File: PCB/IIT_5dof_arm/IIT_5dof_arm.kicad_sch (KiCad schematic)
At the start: 62 parts, among them J1 Screw_Terminal_01x02, J2 Conn_01x06, J3 Conn_01x06, J4 Conn_01x06, J5 Conn_01x06, J6 Conn_01x06, J7 Conn_01x06, J9 DE9_Receptacle_MountingHoles, SW1 SW_MAIN, SW15 SW_MOT, SW17 SW_SPDT, SW18 SW_SPDT, SW19 SW_SPDT, SW20 SW_SPDT, SW21 SW_SPDT, SW22 SW_SPDT, SW23 SW_SPDT, SW24 SW_SPDT, SW25 SW_SPDT, SW26 SW_SPDT, SW27 SW_SPDT, SW28 SW_SPDT, U5 XL8574T, U6 MAX3232, U9 4504

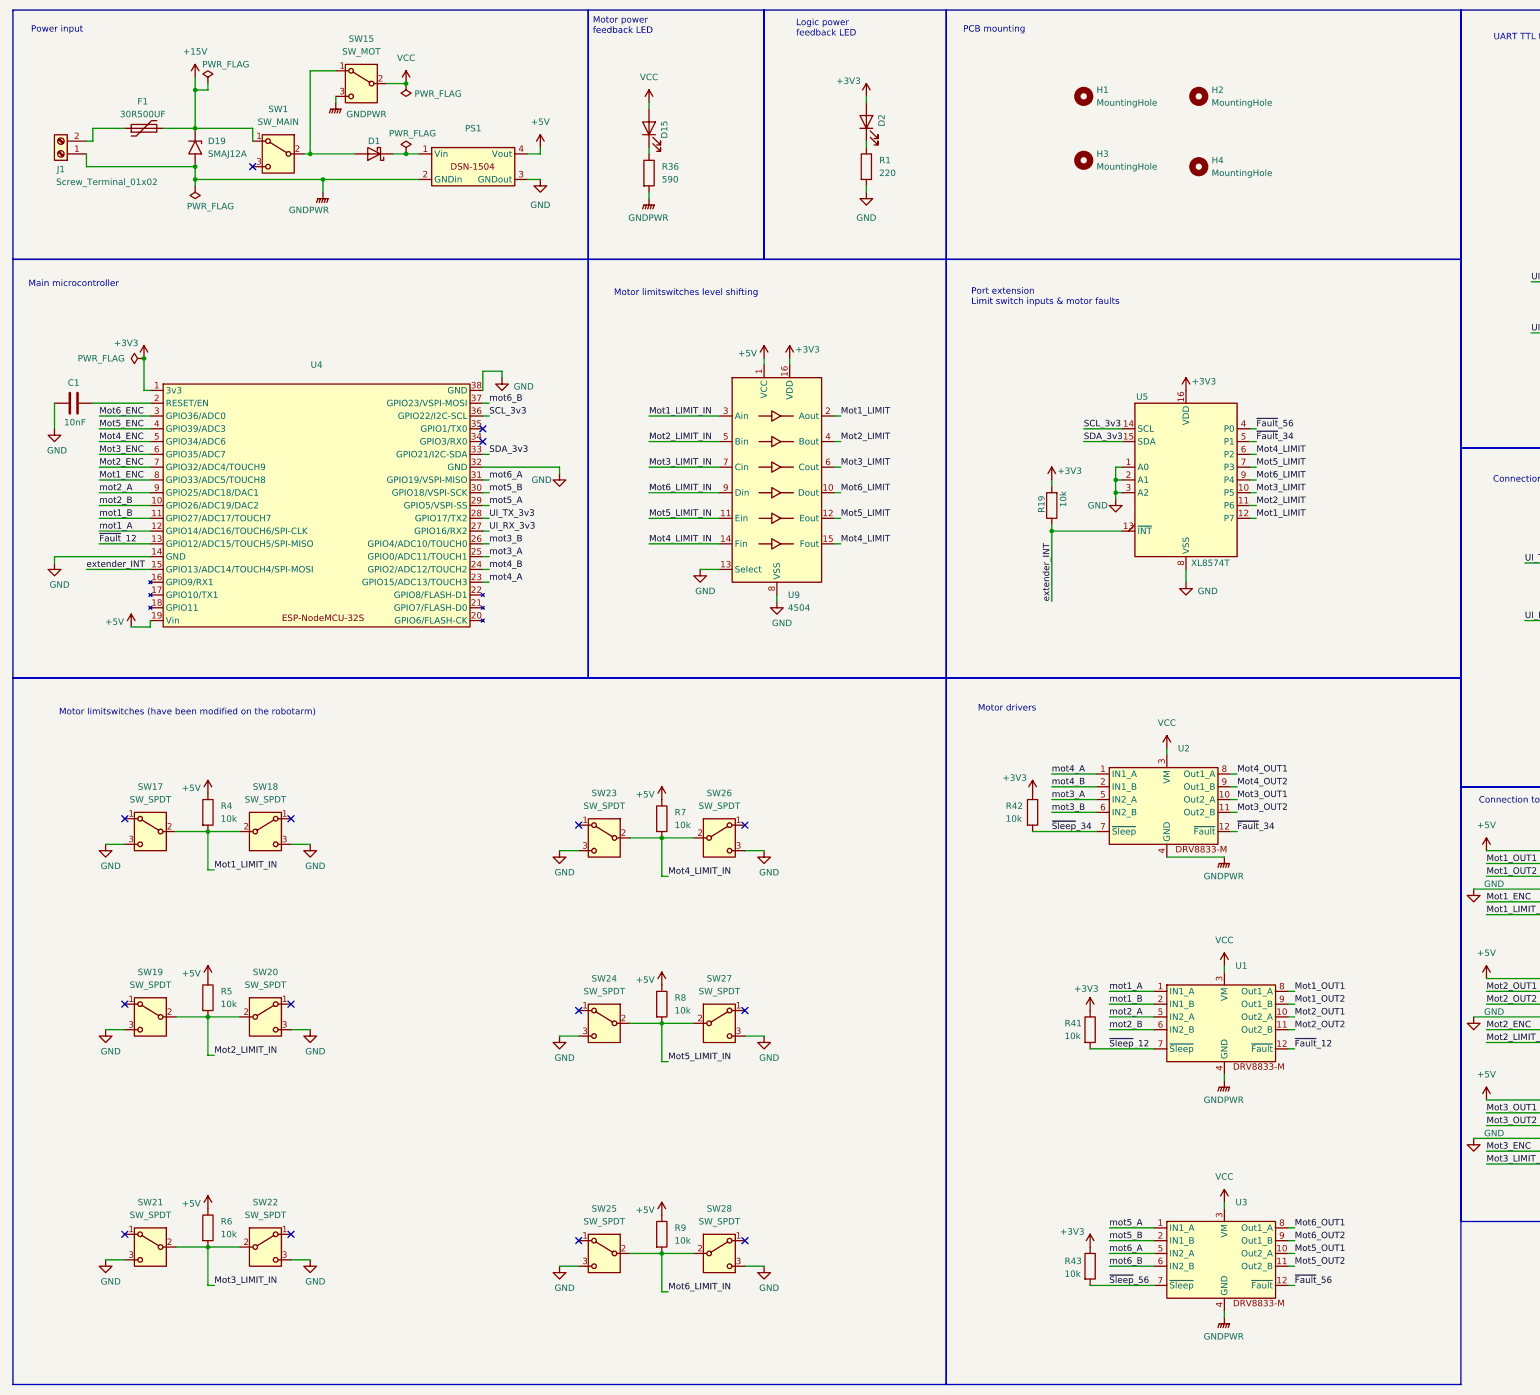
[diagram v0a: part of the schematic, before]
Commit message: Add decoupling capacitors
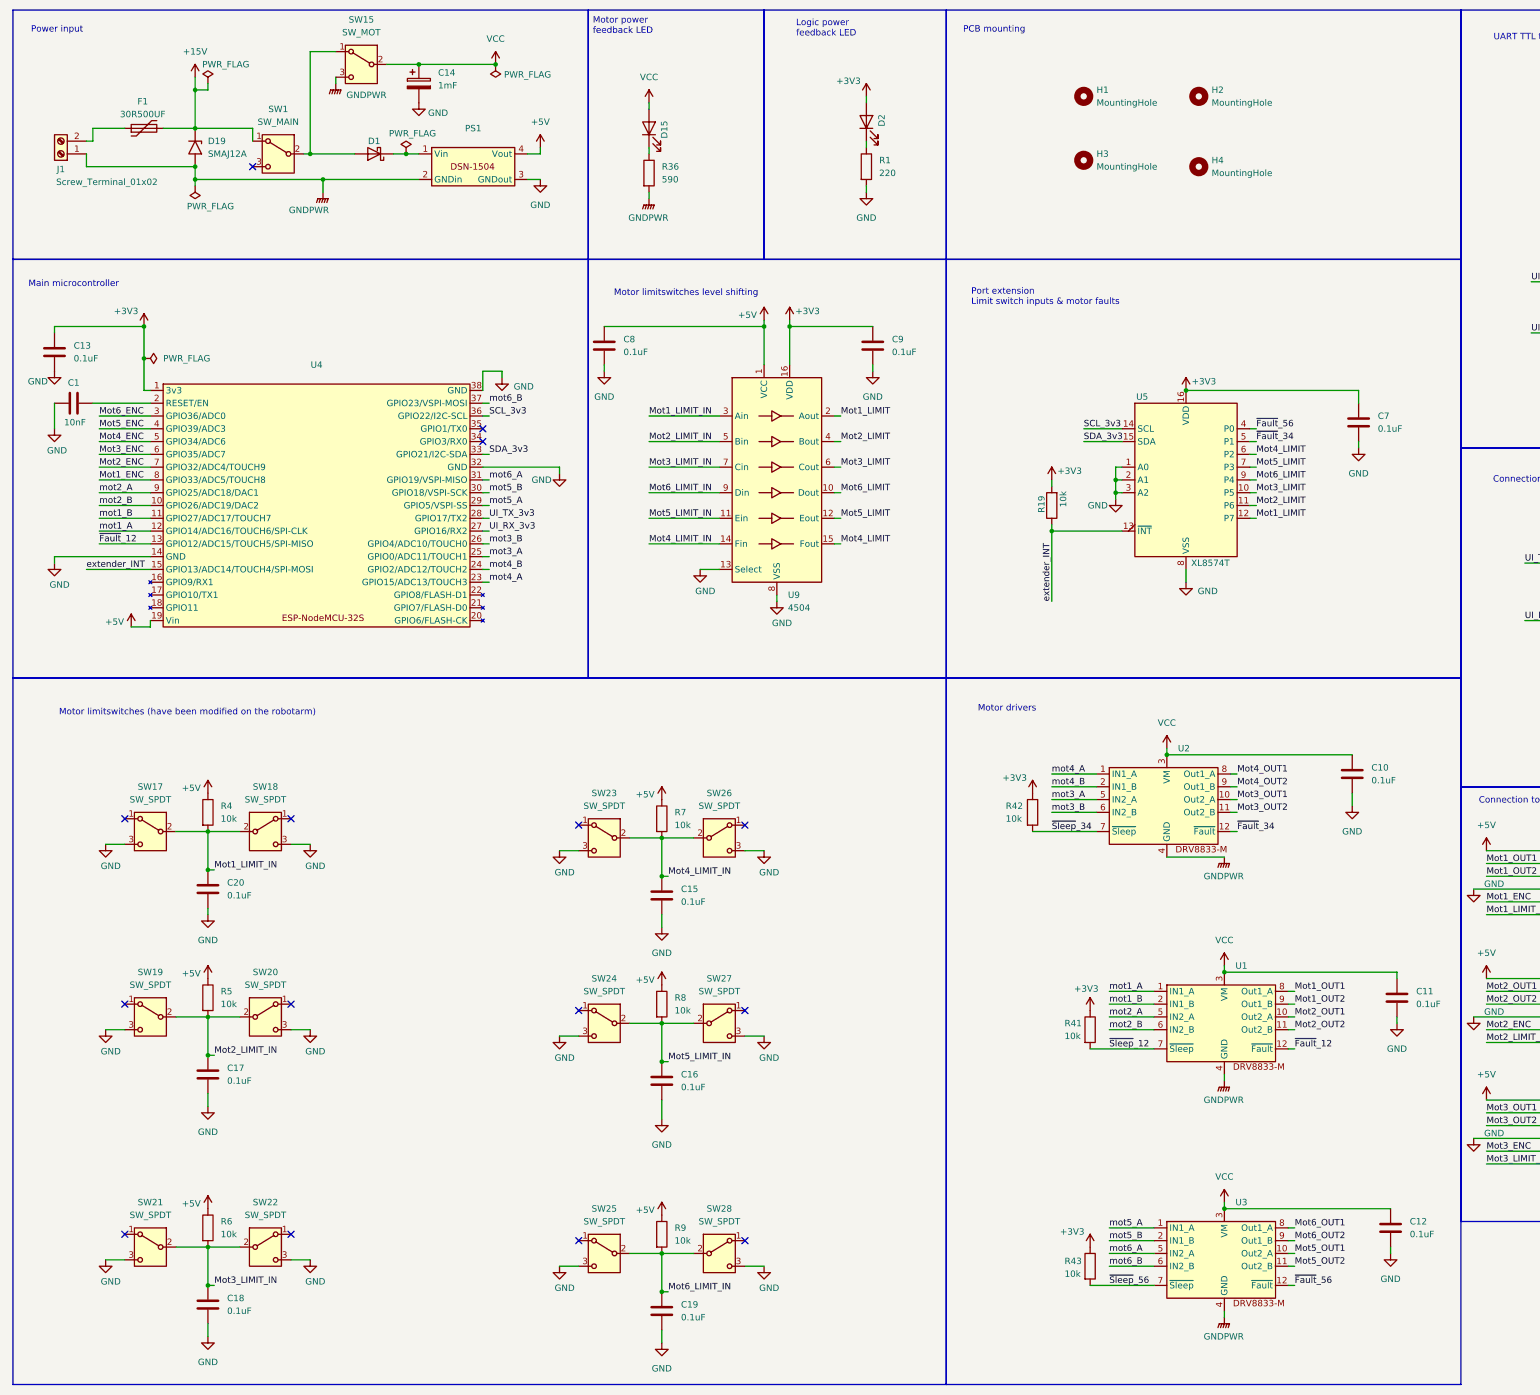
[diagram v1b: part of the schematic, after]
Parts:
- added C10, C11, C12, C13, C15, C16, C17, C18, C19, C20, C7, C8, C9: 0.1uF, Capacitor_SMD:C_0805_2012Metric_Pad1.18x1.45mm_HandSolder, symbol Device:C
- added C14: 1mF, symbol Device:C_Polarized
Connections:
- net +3V3: now also C13.1, C7.1, C9.1
- net +5V: now also C8.1
- net GND: now also C10.2, C11.2, C12.2, C13.2, C14.2, C15.2, C16.2, C17.2, C18.2, C19.2, C20.2, C7.2, C8.2, C9.2
- net Mot1_LIMIT_IN: now also C20.1
- net Mot2_LIMIT_IN: now also C17.1
- net Mot3_LIMIT_IN: now also C18.1
- net Mot4_LIMIT_IN: now also C15.1
- net Mot5_LIMIT_IN: now also C16.1
- net Mot6_LIMIT_IN: now also C19.1
- net VCC: now also C10.1, C11.1, C12.1, C14.1
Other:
- moved on the sheet: SW15

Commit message: Decoupling capacitors layout
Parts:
- C14: value 1mF -> 1000uF; footprint (none) -> Capacitor_THT:C_Radial_D10.0mm_H16.0mm_P5.00mm
- C15, C16, C17, C18, C19, C20: value 0.1uF -> 10nF
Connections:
- net GND: no longer C10.2, C11.2, C12.2, C14.2
- net GNDPWR: now also C10.2, C11.2, C12.2, C14.2

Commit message: Eliminate GNDPWR
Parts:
- C10, C11, C12: value 0.1uF -> 10uF
- D5: value SMAJ12A -> SMAJ5.0A
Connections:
- net GNDPWR is gone; now on net GND: C10.2, C11.2, C12.2, C14.2, D19.2 (A2), J1.1 (Pin_1), PS1.2 (GNDin), R36.2, SW15.3 (C), U1.4 (GND), U2.4 (GND), U3.4 (GND)

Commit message: Update schematic with new functionalities
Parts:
- removed R3: 1k, Resistor_SMD:R_0805_2012Metric_Pad1.20x1.40mm_HandSolder, symbol Device:R
- added C13: 0.1uF, Capacitor_SMD:C_0805_2012Metric_Pad1.18x1.45mm_HandSolder, symbol Device:C
- added D10, D11, D12, D13, D14, D15, D16, D3, D4, D5, D6, D9: LED, LED_THT:LED_D5.0mm, symbol Device:LED
- added J2: Conn_01x02, Connector_PinSocket_2.54mm:PinSocket_1x02_P2.54mm_Vertical, symbol Connector_Generic:Conn_01x02
- added J3: Conn_02x06_Odd_Even, Connector_IDC:IDC-Header_2x06_P2.54mm_Vertical, symbol Connector_Generic:Conn_02x06_Odd_Even
- added J4: Conn_02x08_Odd_Even, Connector_IDC:IDC-Header_2x08_P2.54mm_Vertical, symbol Connector_Generic:Conn_02x08_Odd_Even
- added J5: Conn_02x04_Odd_Even, Connector_IDC:IDC-Header_2x04_P2.54mm_Vertical, symbol Connector_Generic:Conn_02x04_Odd_Even
- added J6: Conn_01x04, Connector_Molex:Molex_KK-254_AE-6410-04A_1x04_P2.54mm_Vertical, symbol Connector_Generic:Conn_01x04
- added K1: G5LE-1, Relay_THT:Relay_SPDT_Omron-G5LE-1, symbol Relay:G5LE-1
- added Q1, Q2: 2N7002, Package_TO_SOT_SMD:SOT-23, symbol Transistor_FET:2N7002
- added R10, R11, R12, R17, R34: 1k, Resistor_SMD:R_0805_2012Metric_Pad1.20x1.40mm_HandSolder, symbol Device:R
- added R13, R16, R29, R31, R33, R9: 10k, Resistor_SMD:R_0805_2012Metric_Pad1.20x1.40mm_HandSolder, symbol Device:R
- added R18, R19, R20, R21, R22, R23: 3k, Resistor_SMD:R_0805_2012Metric_Pad1.20x1.40mm_HandSolder, symbol Device:R
- added R28, R30: 4k7, Resistor_SMD:R_0805_2012Metric_Pad1.20x1.40mm_HandSolder, symbol Device:R
- added R35: 2k, Resistor_SMD:R_0805_2012Metric_Pad1.20x1.40mm_HandSolder, symbol Device:R
- added R7: 220, Resistor_SMD:R_0805_2012Metric_Pad1.20x1.40mm_HandSolder, symbol Device:R
- added R8: 100k, Resistor_SMD:R_0805_2012Metric_Pad1.20x1.40mm_HandSolder, symbol Device:R
- added SW16, SW17: SW_LEVER, symbol Switch:SW_SPST
- added SW8: SW_Push, symbol Switch:SW_Push
- added U2: 74LS157, Package_SO:SO-16_5.3x10.2mm_P1.27mm, symbol 74xx:74LS157
- added U4: XL8574T, Package_SO:SOIC-16W_7.5x10.3mm_P1.27mm, symbol Interface_Expansion:PCF8574
- D7: renamed from D15; footprint Connector_Molex:Molex_KK-254_AE-6410-02A_1x02_P2.54mm_Vertical -> LED_THT:LED_D5.0mm
- D8: renamed from D2; footprint Connector_Molex:Molex_KK-254_AE-6410-02A_1x02_P2.54mm_Vertical -> LED_THT:LED_D5.0mm
- R14: renamed from R36; value 590 -> 10k
- R15: renamed from R1; value 220 -> 1k
- SW12: renamed from SW15; value SW_MOT -> SW_LEVER; footprint Connector_Molex:Molex_KK-254_AE-6410-03A_1x03_P2.54mm_Vertical -> (none)
- SW7: renamed from SW1; value SW_MAIN -> SW_LEVER; footprint Connector_Molex:Molex_KK-254_AE-6410-03A_1x03_P2.54mm_Vertical -> (none)
- U3: renamed from U9; footprint Package_DIP:DIP-16_W7.62mm_Socket_LongPads -> Package_SO:SOIC-16_3.9x9.9mm_P1.27mm
- renumbered C13 to C1, C8 to C10, C9 to C11, C7 to C14, C10 to C15, C11 to C16, C2 to C17, C5 to C18, C6 to C19, C1 to C2, C3 to C20, C4 to C21, C20 to C3, C17 to C4, C18 to C5, C15 to C6, C16 to C7, C19 to C8, C14 to C9, D19 to D1, D4 to D17, D3 to D18, D5 to D19, D1 to D2, J5 to J10, J6 to J11, J7 to J12, J9 to J13, J2 to J7, J3 to J8, J4 to J9, R4 to R1, R5 to R2, R19 to R24, R42 to R25, R41 to R26, R43 to R27, R6 to R3, R2 to R32, R7 to R4, R8 to R5, R9 to R6, SW17 to SW1, SW24 to SW10, SW25 to SW11, SW26 to SW13, SW27 to SW14, SW28 to SW15, SW19 to SW2, SW21 to SW3, SW18 to SW4, SW20 to SW5, SW22 to SW6, SW23 to SW9, U4 to U1, U2 to U6, U1 to U7, U3 to U8, U6 to U9
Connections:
- net +15V: now also J5.1 (Pin_1)
- net +3V3: now also C1.2, C13.1, D3.2 (A), D4.2 (A), D5.2 (A), J3.1 (Pin_1), J3.11 (Pin_11), J3.3 (Pin_3), J3.5 (Pin_5), J3.7 (Pin_7), J3.9 (Pin_9), J4.13 (Pin_13), J4.15 (Pin_15), J4.5 (Pin_5), J4.9 (Pin_9), R28.2, R29.1, R30.2, R31.1, U2.16 (VCC), U4.16 (VDD); no longer C1.1
- net +5V: now also J6.1 (Pin_1), K1.5, R33.1
- net GND: now also C1.1, C13.2, D16.1 (K), J2.2 (Pin_2), J4.12 (Pin_12), J5.6 (Pin_6), J5.8 (Pin_8), J6.4 (Pin_4), Q2.2 (S), R13.2, R16.2, R18.2, R19.2, R20.2, R21.2, R22.2, R23.2, R35.2, R8.2, R9.2, SW16.1 (A), SW17.1 (A), SW8.2, U2.8 (GND), U4.2 (A1), U4.3 (A2), U4.8 (VSS); no longer C1.2, SW12.3 (C)
- net Mot1_ENC: now also U2.13 (I1d), U2.5 (I0b); no longer U1.8 (GPIO33/ADC5/TOUCH8)
- net Mot1_LIMIT_IN: now also D15.2 (A)
- net Mot2_ENC: now also U1.8 (GPIO33/ADC5/TOUCH8); no longer U1.7 (GPIO32/ADC4/TOUCH9)
- net Mot2_LIMIT_IN: now also D14.2 (A)
- net Mot3_ENC: now also U1.7 (GPIO32/ADC4/TOUCH9); no longer U1.6 (GPIO35/ADC7)
- net Mot3_LIMIT_IN: now also D13.2 (A)
- net Mot4_ENC: now also U1.6 (GPIO35/ADC7); no longer U1.5 (GPIO34/ADC6)
- net Mot4_LIMIT_IN: now also D12.2 (A)
- net Mot5_ENC: now also U1.5 (GPIO34/ADC6); no longer U1.4 (GPIO39/ADC3)
- net Mot5_LIMIT_IN: now also D11.2 (A)
- net Mot6_ENC: now also U1.4 (GPIO39/ADC3); no longer U1.3 (GPIO36/ADC0)
- net Mot6_LIMIT_IN: now also D10.2 (A)
- net SCL_3v3: now also R28.1, U4.14 (SCL)
- net SDA_3v3: now also R30.1, U4.15 (SDA)
- net VCC: now also J4.3 (Pin_3), J5.4 (Pin_4), K1.3; no longer C12.1, C15.1, C16.1, U6.3 (VM), U7.3 (VM), U8.3 (VM)
- net extender_INT: now also U4.13 (~{INT})
- net mot1_A: now also U2.4 (Za); no longer U1.12 (GPIO14/ADC16/TOUCH6/SPI-CLK)
- net mot1_B: now also U1.12 (GPIO14/ADC16/TOUCH6/SPI-CLK); no longer U1.11 (GPIO27/ADC17/TOUCH7)
- net mot2_A: now also U1.10 (GPIO26/ADC19/DAC2); no longer U1.9 (GPIO25/ADC18/DAC1)
- net mot2_B: now also U1.11 (GPIO27/ADC17/TOUCH7); no longer U1.10 (GPIO26/ADC19/DAC2)
- net ~{Fault}_12: now also U4.4 (P0); no longer U1.13 (GPIO12/ADC15/TOUCH5/SPI-MISO)
- net EspRST: now reaches C2.2, U1.2 (RESET/EN)
- net EspRST: now also J2.1 (Pin_1), SW8.1
- net EMG_signal_5V: now reaches J13.7
- net EMG_signal_5V: now also R33.2, R34.1, SW17.2 (B)
- net LED_VCC-: now reaches D7.1 (K), R14.1
- net LED_VCC-: now also J4.4 (Pin_4)
- net LED_3v3-: now reaches D8.1 (K), R15.1
- net LED_3v3-: now also J4.6 (Pin_6)
- net PowerOn: now reaches D2.2 (A), SW12.1 (A), SW7.2 (B)
- net PowerOn: now also D6.2 (A), J4.1 (Pin_1), J5.2 (Pin_2), J5.3 (Pin_3)
- new net: R29.2, U4.1 (A0)
- new net: Q2.1 (G), R7.2, R8.1
- new net: Q1.2 (S), Q2.3 (D)
- new net: K1.2, Q1.3 (D)
- new net: R9.1, U2.11 (I0c), U2.14 (I0d), U2.15 (E)
- new net EMG_LED-: D3.1 (K), J4.10 (Pin_10), R10.1
- new net EMG_signal: J5.5 (Pin_5), Q1.1 (G), R10.2, R34.2, R35.1, U1.3 (GPIO36/ADC0)
- new net ESP-CAM/RX: J6.2 (Pin_2), U2.6 (I1b)
- new net ESP-CAM/TX: J6.3 (Pin_3), U2.9 (Zc)
- new net LED_MotPower-: D9.1 (K), J4.8 (Pin_8), R16.1
- new net LED_PowerOn-: D6.1 (K), J4.2 (Pin_2), R13.1
- new net Limit1_LED-: D15.1 (K), J3.2 (Pin_2), R23.1
- new net Limit2_LED-: D14.1 (K), J3.4 (Pin_4), R22.1
- new net Limit3_LED-: D13.1 (K), J3.6 (Pin_6), R21.1
- new net Limit4_LED-: D12.1 (K), J3.8 (Pin_8), R20.1
- new net Limit5_LED-: D11.1 (K), J3.10 (Pin_10), R19.1
- new net Limit6_LED-: D10.1 (K), J3.12 (Pin_12), R18.1
- new net Man/Aut SW: J5.7 (Pin_7), R31.2, SW16.2 (B), U4.5 (P1)
- new net Mot1_ENC/ESP-CAM_RX: U1.9 (GPIO25/ADC18/DAC1), U2.7 (Zb)
- new net MotEnable: R7.1, U4.6 (P2)
- new net MotPower: C12.1, C15.1, C16.1, D9.2 (A), J4.7 (Pin_7), K1.1, U6.3 (VM), U7.3 (VM), U8.3 (VM)
- new net TBD_Led1: R11.2, U4.11 (P6)
- new net TBD_Led1-: D4.1 (K), J4.14 (Pin_14), R11.1
- new net TBD_Led2: R12.2, U4.12 (P7)
- new net TBD_Led2-: D5.1 (K), J4.16 (Pin_16), R12.1
- new net alt_mot1A: U2.3 (I1a), U4.9 (P4)
- new net alt_mot1_enc: U2.12 (Zd), U4.10 (P5)
- new net mot1_A/ESP-CAM_TX: U1.13 (GPIO12/ADC15/TOUCH5/SPI-MISO), U2.10 (I1c), U2.2 (I0a)
- new net useESP-CAM: R17.1, U2.1 (S), U4.7 (P3)
- new net useESP-CAM_LED+: D16.2 (A), J4.11 (Pin_11), R17.2
- no-connect marks 19 -> 22
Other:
- note added: "ESP-CAM serial interface"
- note added: "Emergency signal"
- note added: "Feedback LEDs"
- note added: "Manual/automatic switch"
- note added: "Motor current relay"
- note added: "Switch ESP-CAM signals"
- note added: "Switch connector"
- note removed: "Logic power feedback LED"
- note removed: "Motor power feedback LED"
- moved on the sheet: C1, C10, C11, C12, C14, C15, C16, C17, C18, C19, C2, C20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
